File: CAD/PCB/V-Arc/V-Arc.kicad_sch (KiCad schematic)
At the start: 0 parts

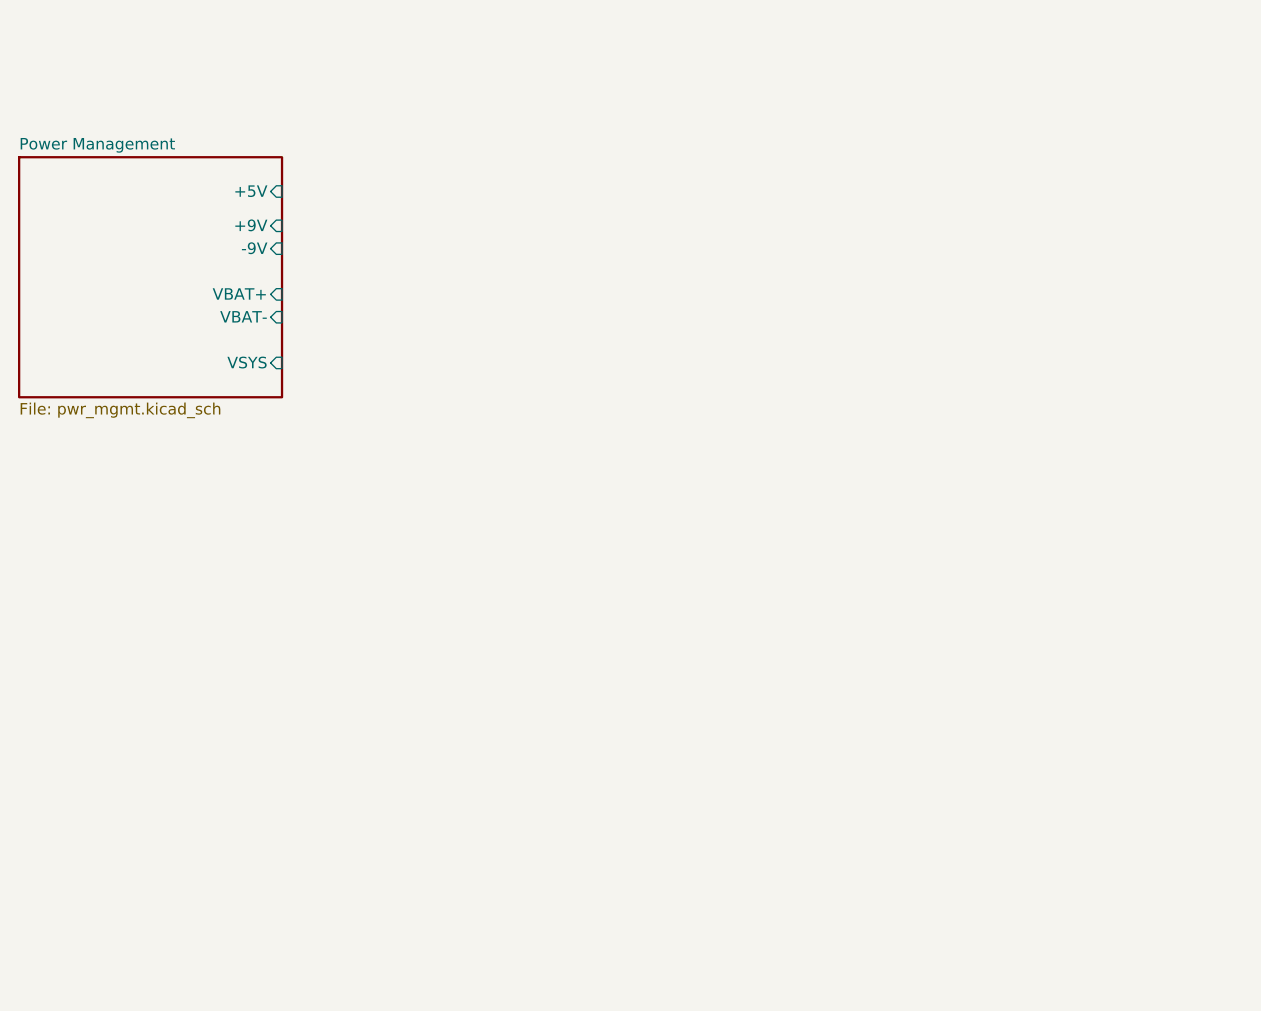
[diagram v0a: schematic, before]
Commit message: Added more sheets to the schematic
-Added audio front end sheet
-Added Daisy Seed 3 core sheet
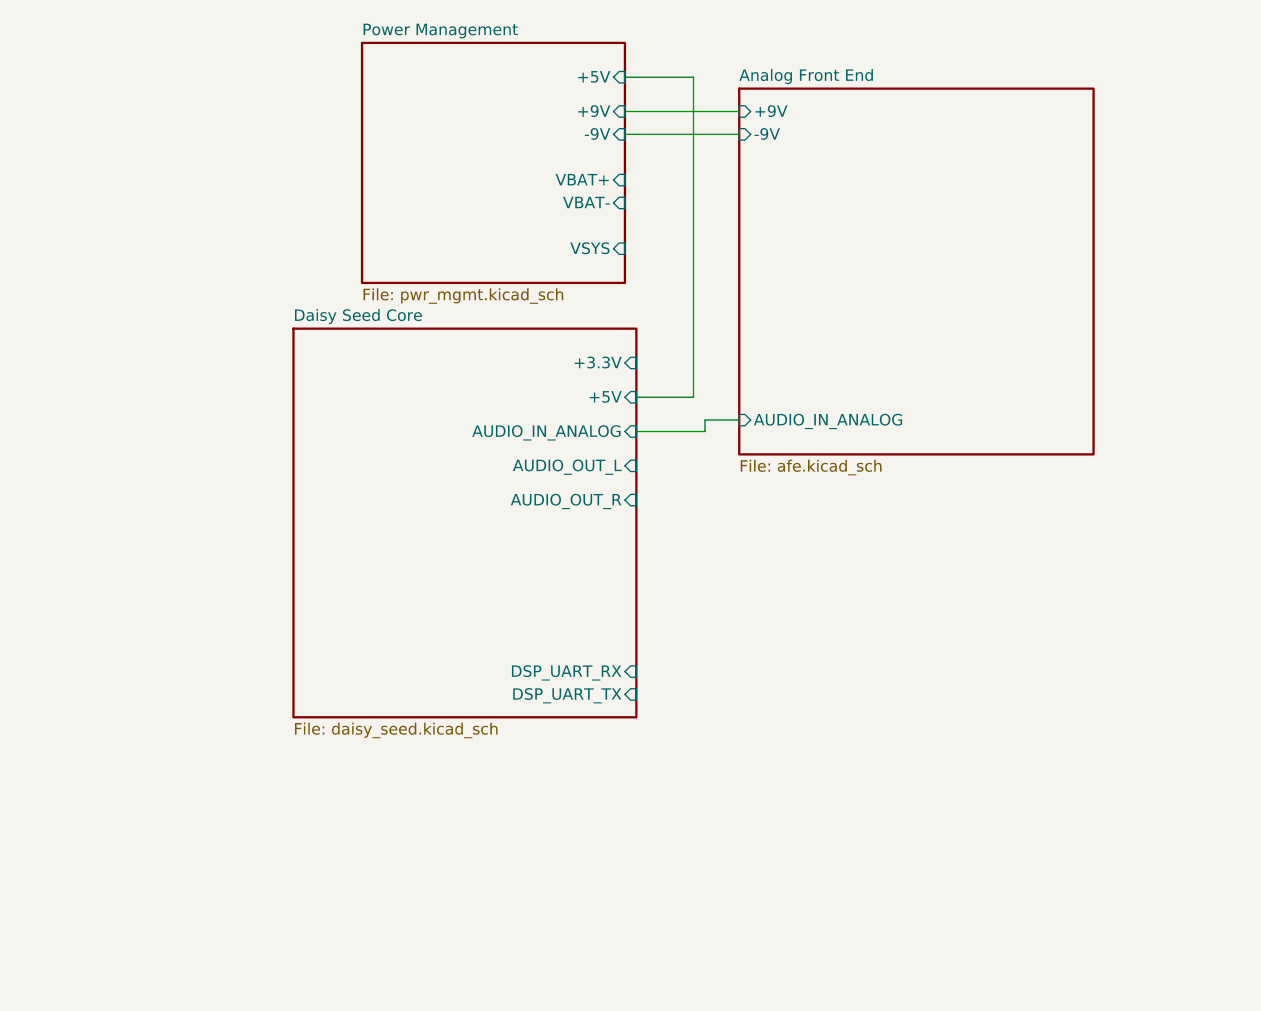
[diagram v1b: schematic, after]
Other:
- added sheet Analog Front End (afe.kicad_sch)
- added sheet Daisy Seed Core (daisy_seed.kicad_sch)

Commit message: Added a sheet and organized
-Added XIAO ESP32 Core sheet
-Titled all sheets
-Added power switch to the power sheet
-Organized all sheets with text boxes
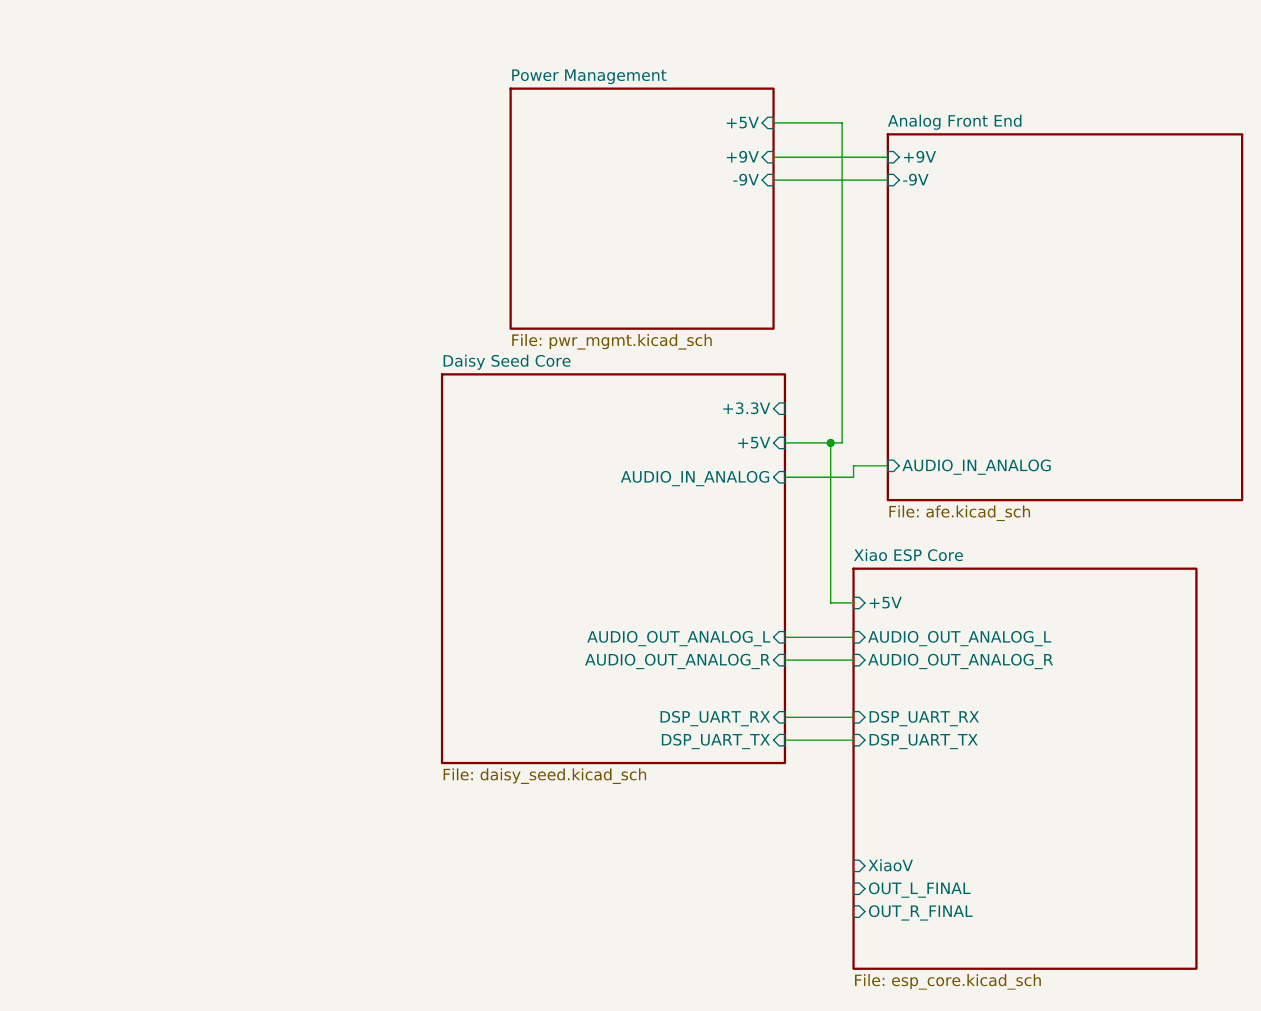
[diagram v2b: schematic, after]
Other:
- added sheet Xiao ESP Core (esp_core.kicad_sch)
- sheet Daisy Seed Core ports: added AUDIO_OUT_ANALOG_L, AUDIO_OUT_ANALOG_R; removed AUDIO_OUT_L, AUDIO_OUT_R
- sheet Power Management ports: added none; removed VBAT+, VBAT-, VSYS
